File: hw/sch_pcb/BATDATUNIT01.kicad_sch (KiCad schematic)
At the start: 45 parts, among them J1 USBC_USB4105-GF-A, J2 46436-9327, U1 FT260Q-T, U2 USBLC6-2SC6, U3 TCA4307, U4 SHT35-DIS, U5 PCA9541ABS/01

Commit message: WIP, schematic improvements, bigger page, reststructualized
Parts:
- added BZ1: LET9032ES-03L, MLAB_BUZZER:MagneticBuzzer_LET9032ES-03L-2.7-16-R, symbol Device:Buzzer
- added C26, C27, C36, C44, C5, C6, C60, C7: 100n, Capacitor_SMD:C_0805_2012Metric, symbol Device:C_Small
- added C30, C33: 15p, Capacitor_SMD:C_0805_2012Metric, symbol Device:C_Small
- added C40: 10u, Capacitor_SMD:C_0805_2012Metric, symbol Device:C_Small
- added C43: 4u7, Capacitor_SMD:C_0805_2012Metric, symbol Device:C_Small
- added C47: 1u, Capacitor_SMD:C_0805_2012Metric, symbol Device:C_Small
- added D16 (x3): ORANGE, Mlab_D:SMD_LED_RIGHT_KINGBRIGHT_1605, symbol Device:LED_Small
- added IC1: MAX14502AETL+, Mlab_IO:QFN40P500X500X80-41N, symbol MLAB_IO:MAX14502AETL+
- added J22: HEADER_2x03, Mlab_Pin_Headers:SMD_2x03, symbol MLAB_HEADER:HEADER_2x03
- added J9: SD_Card-FPS009-4200-0, Mlab_CON:FPS009-4200-0, symbol MLAB_CONNECTORS:SD_Card-FPS009-4200-0
- added JP2: Jumper_3_Bridged12, Jumper:SolderJumper-3_P1.3mm_Bridged2Bar12_RoundedPad1.0x1.5mm, symbol Jumper:SolderJumper_3_Bridged12
- added Q1, Q2, Q3, Q4: BC817-25, Package_TO_SOT_SMD:SOT-23-3, symbol Device:Q_NPN_BEC
- added R1: 6.19k, Resistor_SMD:R_0805_2012Metric, symbol Device:R_Small
- added R16, R17, R28, R29, R55, R56: 1k, Resistor_SMD:R_0805_2012Metric, symbol Device:R_Small
- added R17 (x6): 100R, Resistor_SMD:R_0805_2012Metric, symbol SPACEDOS02A_PCB01A-rescue:R-device-DATALOGGER01A-rescue-CCP2019V01A-rescue-SPAC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
- added R23 (x2), R58, R59, R60: 10k, Resistor_SMD:R_0805_2012Metric, symbol Device:R_Small
- added R54 (x3): 270R, Resistor_SMD:R_0805_2012Metric, symbol Device:R_Small
- added SW3: SKRTLAE010, Mlab_SW:SKRT, symbol MLAB_SW:SW_Push_shield
- added SW3, SW4: KMT031, Mlab_SW:KMT031 NGJ LHS C&K, symbol Switch:SW_Push
- added U10: ATMEGA1284P-AU, Package_QFP:TQFP-44_10x10mm_P0.8mm, symbol SPACEDOS01A_PCB01A-rescue:ATMEGA1284P-AU-atmel-DATALOGGER01A-rescue-CCP2019V01A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
- added U11: PCF85263A, Package_SO:TSSOP-10_3x3mm_P0.5mm, symbol MLAB_IO:PCF85263A
- added U12: TMUX1574DYYR, Mlab_IO:SOT-23-16 THIN, symbol MLAB_IO:TMUX1574DYYR
- added U6: AT24CS64-SSHM, Package_SO:SOIC-8_3.9x4.9mm_P1.27mm, symbol Memory_EEPROM:AT24CS64-SSHM
- added Y1: 8 MHz, Crystal:Crystal_SMD_3225-4Pin_3.2x2.5mm, symbol Device:Crystal_GND24_Small
- added Y2: ABS07-120-32.768KHZ-T, Mlab_XTAL:ABS07, symbol SPACEDOS01A_PCB01A-rescue:Crystal-device-DATALOGGER01A-rescue-CCP2019V01A-rescue
- R20, R21: symbol SPACEDOS01A_PCB01A-rescue:R-device-DATALOGGER01A-rescue-CCP2019V01A-rescue -> Device:R_Small
- renumbered C3 to C4, J2 to J4, R1 to R13, R10 to R14, R2 to R15, R11 to R18, R5 to R26, R16 to R27, R6 to R31, R7 to R32, TP2 to TP1, U3 to U10, U1 to U3, U5 to U4, U4 to U6
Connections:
- net +3.3V: now also BZ1.1 (-), C26.1, C27.1, C36.1, C47.1, C6.1, D16.2 (A), D16.2 (A), D16.2 (A), IC1.39 (VCC), IC1.5 (VIO), IC1.9 (~{RST}), J22.2, JP2.1 (A), R23.2, R58.1, R59.1, U10.17 (VCC), U10.27 (AVCC), U10.38 (VCC), U10.5 (VCC), U11.10 (VDD), U12.16 (VDD), U6.8 (VCC)
- net DET_I2C_EN: now also U10.42 ((PCINT10/AIN0/INT2)PB2)
- net EXT_A0: now also U10.37 ((PCINT0/ADC0)PA0)
- net EXT_A1: now also U10.36 ((PCINT1/ADC1)PA1)
- net EXT_B0: now also U10.40 ((PCINT8/T0/XCK)PB0)
- net EXT_B1: now also U10.41 ((PCINT9/CLKO/T1)PB1)
- net EXT_C0: now also U10.25 ((PCINT22/TOSC1)PC6)
- net EXT_C1: now also U10.26 ((PCINT23/TOSC2)PC7)
- net EXT_MISO: now also U12.6 (S2B)
- net EXT_MOSI: now also U12.3 (S1B)
- net EXT_RX: now also U10.11 ((PCINT26/RXD1/INT0)PD2)
- net EXT_SCLK: now also U12.10 (S3B)
- net EXT_TX: now also U10.12 ((PCINT27/TXD1/INT1)PD3)
- net GND: now also C26.2, C27.2, C30.2, C33.2, C36.2, C40.2, C44.2, C47.2, C5.2, C6.2, C60.2, C7.2, IC1.18 (GND_1), IC1.24 (GND_2), IC1.26 (GND_3), IC1.33 (CCRD_PRST), IC1.35 (N.C._1), IC1.36 (N.C._2), IC1.37 (GND_4), IC1.4 (ADD), IC1.41 (GND_5), J22.6, J9.12 (SHELL1), J9.3 (VSS), J9.6 (VSS), JP2.3 (B), Q1.2 (E), Q2.2 (E), Q3.2 (E), Q4.2 (E), R1.2, R23.1, R56.2, R60.1, SW3.2, SW3.2, SW3.GND (SHIELD), SW4.1, U10.18 (GND), U10.28 (GND), U10.39 (GND), U10.6 (GND), U11.5 (GND), U12.15 (~{EN}), U12.8 (GND), U6.1 (A0), U6.2 (A1), U6.3 (A2), U6.4 (GND), U6.7 (WP), Y1.2, Y1.4
- net MCU_RXD: now also U10.9 ((PCINT24/RXD0)PD0)
- net MCU_TXD: now also U10.10 ((PCINT25/TXD0)PD1)
- net RST#: now also C43.2
- net SCL_I2C: now also IC1.2 (SCL), U11.7 (SCL), U6.6 (SCL)
- net SCL_MCU: now also U10.19 ((PCINT16/SCL)PC0)
- net SDA_I2C: now also IC1.3 (SDA), U11.6 (SDA), U6.5 (SDA)
- net SDA_MCU: now also U10.20 ((PCINT17/SDA)PC1)
- net USB_D+: now also IC1.22 (CD+)
- net USB_D-: now also IC1.21 (CD-)
- net USB_FTDI_D+: now also IC1.20 (HD+)
- net USB_FTDI_D-: now also IC1.19 (HD-)
- net VBUS: now also R55.1
- new net: IC1.28 (KVBUS), R55.2, R56.1
- new net: D16.1 (K), R54.1 (x3)
- new net: Q2.3 (C), R54.2
- new net: J9.1 (CD/DAT3), R17.2
- new net: C40.1, C44.1, U10.29 (AREF)
- new net: C30.1, U10.7 (XTAL2), Y1.1
- new net: C33.1, U10.8 (XTAL1), Y1.3
- new net: C60.1, U11.3 (VBAT)
- new net: Q3.1 (B), R28.2
- new net: IC1.1 (I2C_SEL), JP2.2 (C)
- new net: J9.7 (DAT0), R17.1
- new net: J9.9 (DAT2), R17.2
- new net: Q3.3 (C), R54.2
- new net: J9.2 (CMD), R17.2
- new net: BZ1.2 (+), Q4.3 (C)
- new net: J9.5 (CLK), R17.2
- new net: J9.8 (DAT1), R17.1
- new net: Q1.1 (B), R16.2
- new net: Q1.3 (C), R54.2
- new net: Q4.1 (B), R29.2
- new net: U11.1 (OSCI), Y2.2
- new net: U11.2 (OSCO), Y2.1
- new net: Q2.1 (B), R17.2
- new net 3v3_SD: IC1.40 (VSD), J9.4 (VDD)
- new net 3v3_SD_CTRL: U10.22 ((PCINT19/TMS)PC3)
- new net BTN_USER_A: R58.2, SW3.1, U10.31 ((PCINT6/ADC6)PA6)
- new net BTN_USER_B: R59.2, SW3.1, U10.30 ((PCINT7/ADC7)PA7)
- new net CCLK: IC1.32 (CCLK1), R17.1
- new net CCMD: IC1.34 (CCMD1), R17.1
- new net CDAT0: IC1.13 (CDAT1_0), R17.2
- new net CDAT1: IC1.12 (CDAT1_1), R17.2
- new net CDAT2: IC1.11 (CDAT1_2), R17.1
- new net CDAT3: IC1.10 (CDAT1_3), R17.1
- new net CLDO: C5.1, IC1.38 (CLDO)
- new net CS_SD: IC1.14 (HDAT1_3), U10.44 ((PCINT12/OC0B/~{SS})PB4)
- new net LED_U1: R16.1, U10.13 ((PCINT28/XCK1/OC1B)PD4)
- new net LED_U2: R28.1, U10.14 ((PCINT294/OC1A)PD5)
- new net LED_U3: R17.1, U10.15 ((PCINT30/OC2B/ICP)PD6)
- new net MISO_MCU: J22.1, U10.2 ((PCINT14/MISO)PB6), U12.7 (D2)
- new net MISO_SD: IC1.17 (HDAT1_0), U12.5 (S2A)
- new net MOSI_MCU: J22.4, U10.1 ((PCINT13/MOSI)PB5), U12.4 (D1)
- new net MOSI_SD: IC1.31 (HCMD1), U12.2 (S1A)
- new net RREF: IC1.27 (RREF), R1.1
- new net RST#_P: C43.1, J22.5, R23.1, SW4.2, U10.4 (~{RESET})
- new net SCLK_MCU: J22.3, U10.3 ((PCINT15/SCK)PB7), U12.9 (D3)
- new net SCLK_SD: IC1.29 (HCLK1), U12.11 (S3A)
- new net SPI_MUX_SEL: R60.2, U10.21 ((PCINT18/TCK)PC2), U12.1 (SEL)
- new net VTM: C7.1, IC1.23 (VTM)
- new net buzzer: R29.1, U10.16 ((PCINT31/OC2A)PD7)
- new net mode: IC1.8 (MODE), R23.2, U10.43 ((PCINT11/AIN1/OC0)PB3)
- no-connect marks 26 -> 43
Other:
- removed sheet mcu
- note added: "ATmega 1284p microcontroller"
- note added: "Connector for detector board"
- note added: "FTDI (USB to UART and I2C)"
- note added: "I2C master selector (from FTDI or ATmega)"
- note added: "I2C sensors and accessories (hygrometer, altimeter, eeprom, RTC)"
- note added: "Mechanical"
- note added: "SD card interface (USB to SDcard reader and USB-bridge to FTDI)"
- note added: "SPI-MUX (switching SPI from MCU to SDcard or to detector ext. connector)"
- note added: "USB-C connector and ESD protection"
- note added: "User interface (LED indicators, Buttons)"
- note removed: "USB-C connector"
- moved on the sheet: C4, C?, D1, D2, FID1, FID2, FID3, FID4, H1, H2, H3, H4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

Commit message: Updates in schematics, improved readability
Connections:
- net EXT_I2C_EN: now reaches U10.23 ((PCINT20/TDO)PC4)
- net EXT_I2C_EN: now also R21.1, U10.1 (EN)
- net EXT_PWR_5v_EN: now reaches U10.35 ((PCINT2/ADC2)PA2)
- removed net DET_I2C_EN: R21.1, U10.1 (EN), U10.42 ((PCINT10/AIN0/INT2)PB2)
- net EXT_I2C_SCL renamed SCL_OUT
- net EXT_I2C_SDA renamed SDA_OUT
- net EXT_MISO renamed MISO_OUT
- net EXT_MOSI renamed MOSI_OUT
- net EXT_SCLK renamed SCLK_OUT
- net MCU_RXD renamed USB_TXD
- net MCU_TXD renamed USB_RXD
- new net EXT_PWR_3v3_EN: U10.42 ((PCINT10/AIN0/INT2)PB2)
- no-connect marks 43 -> 42
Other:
- company: MLAB.cz -> MLAB.cz, roman-dvorak
- moved on the sheet: C?, D1, D2, IC1, JP1, JP2, R13, R14, R15, R18, R23, R26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

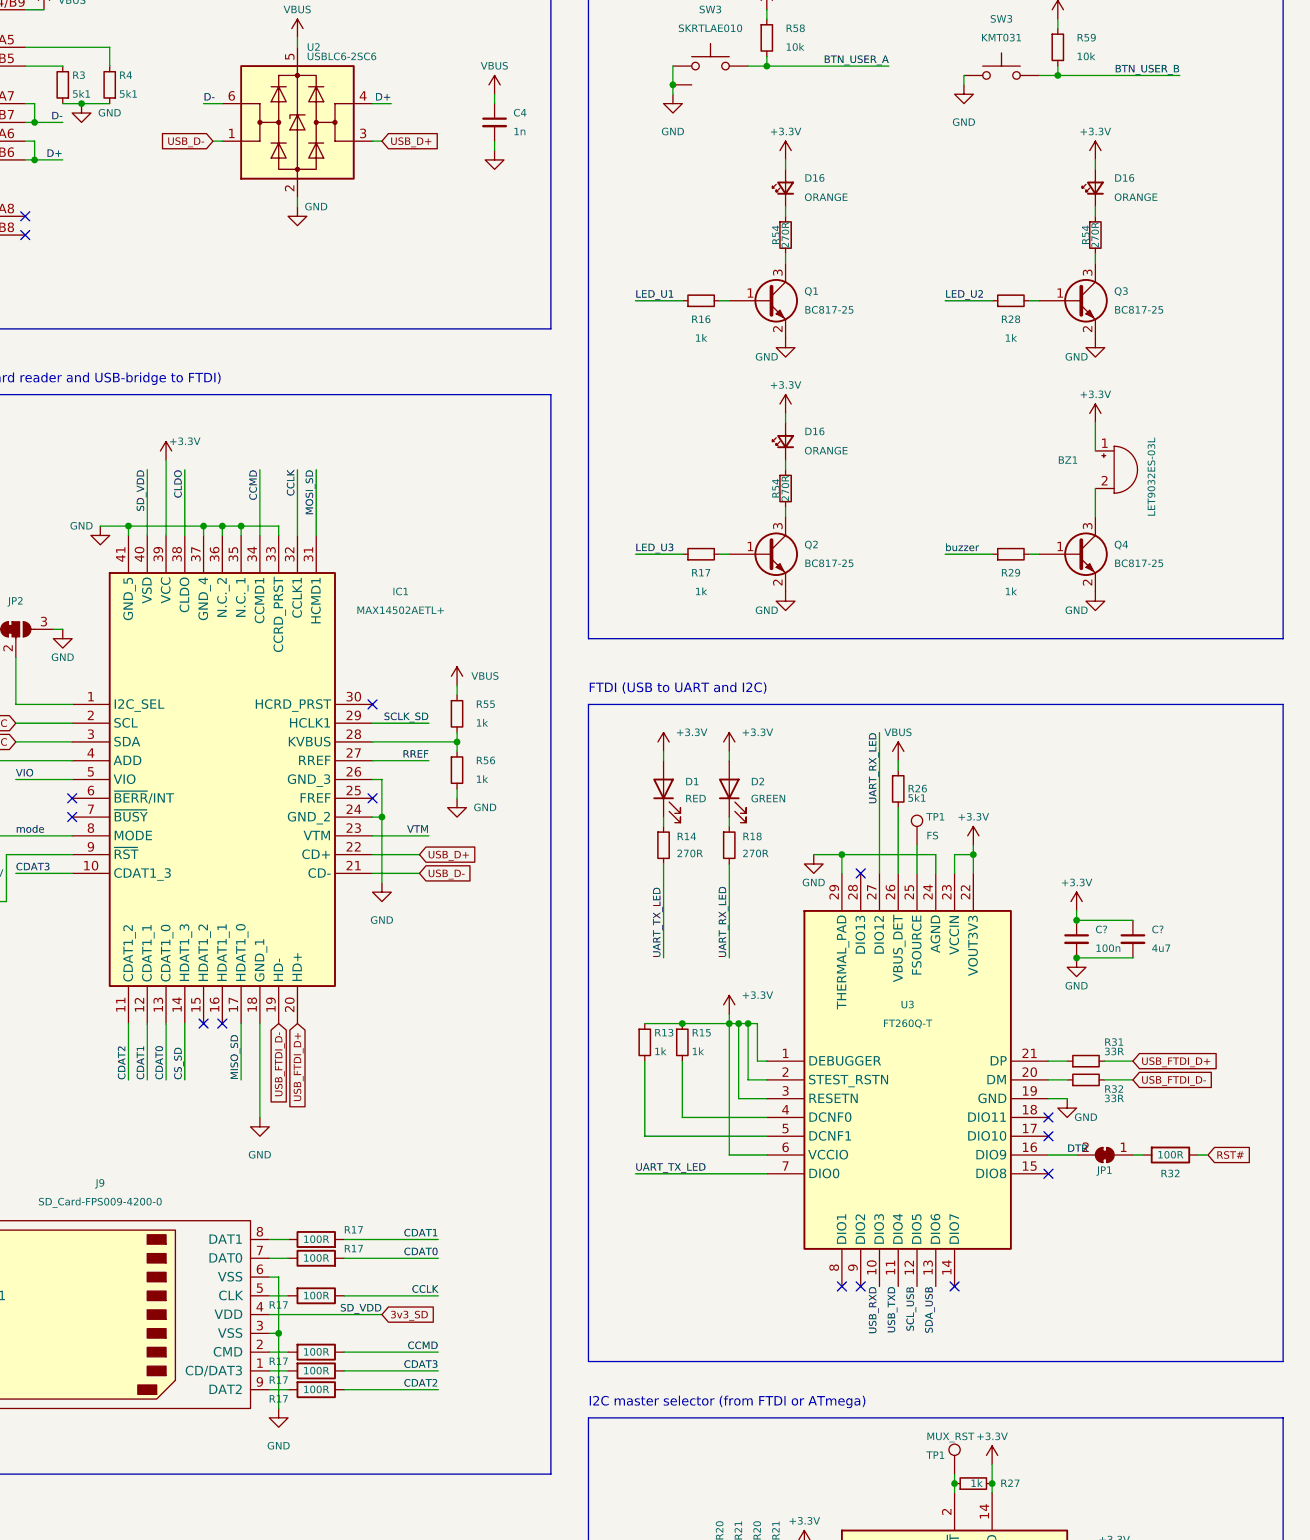
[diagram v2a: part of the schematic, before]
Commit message: minor updates, update kibot
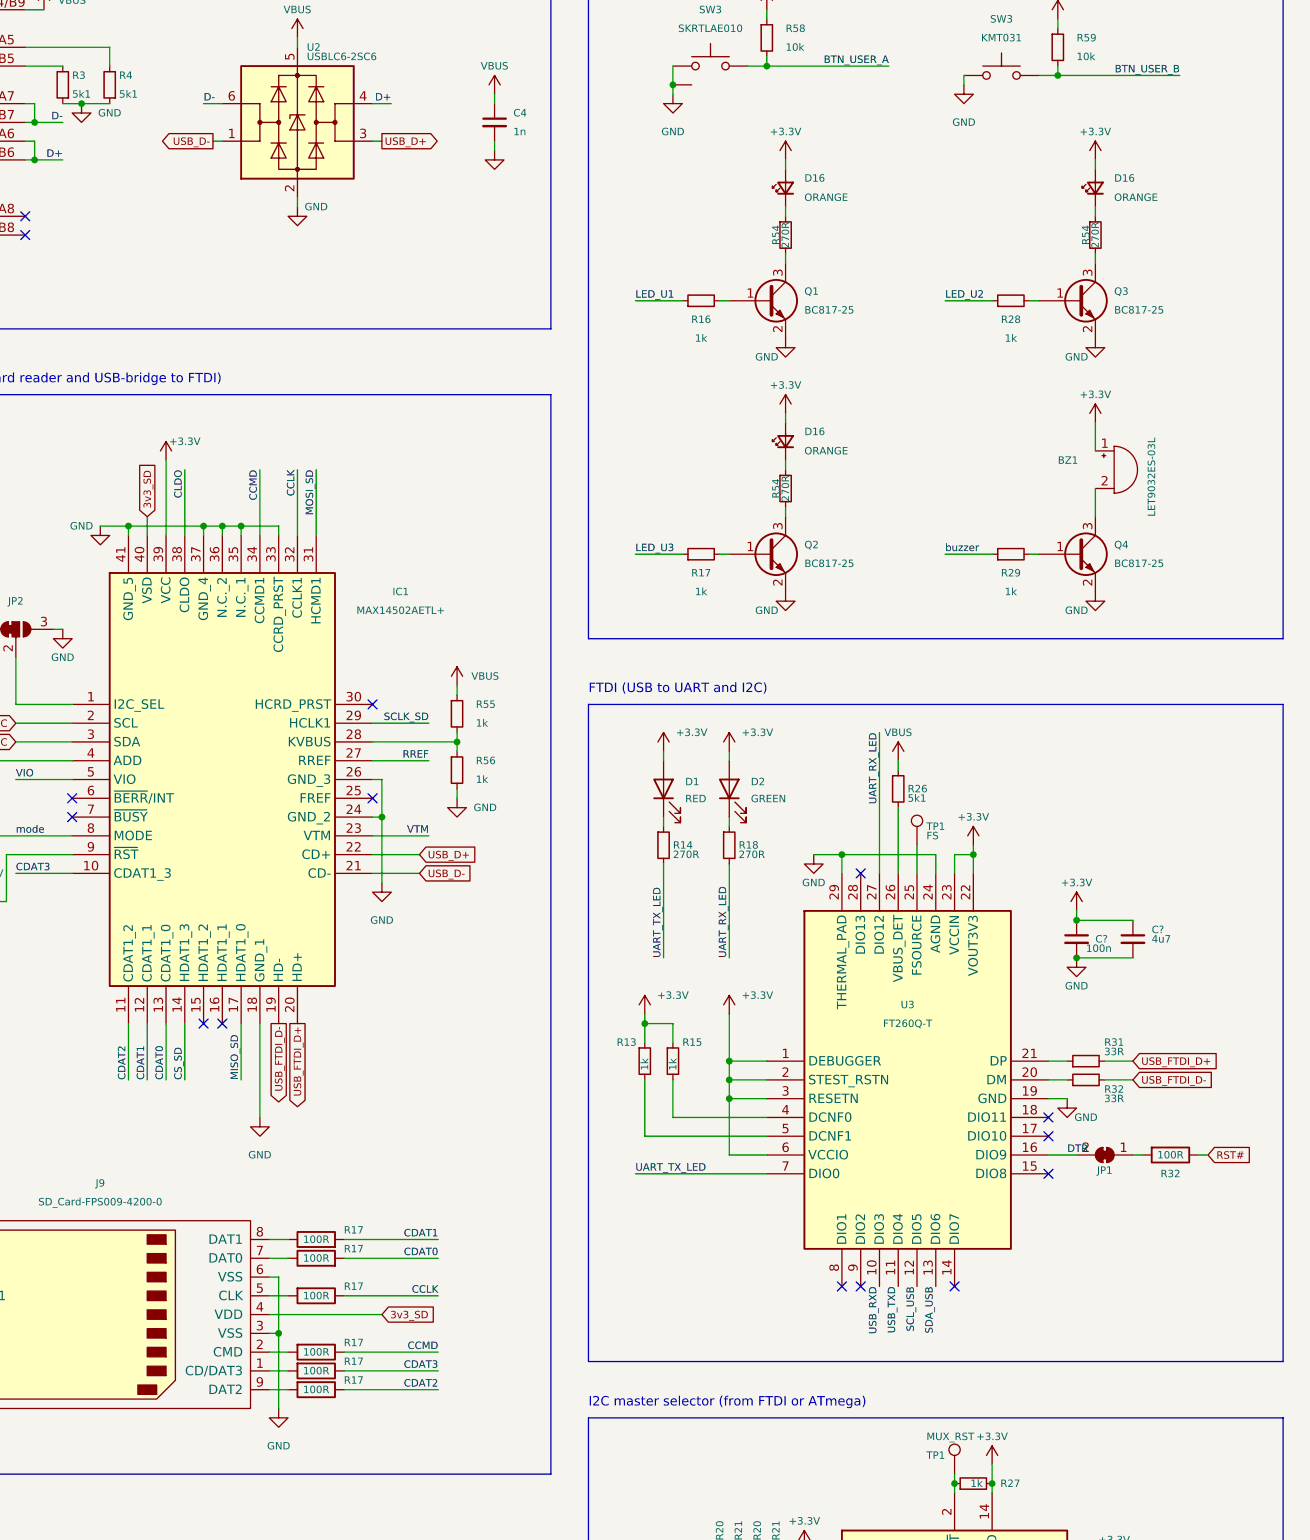
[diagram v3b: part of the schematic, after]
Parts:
- D1: UST_ID (none) -> 65481f96462c6d9e72056b54
- D16: UST_ID (none) -> 65481fdd462c6d9e72056b6a
- D2: UST_ID (none) -> 65481f0c462c6d9e72056b3d
- IC1: UST_ID (none) -> 6548165f462c6d9e720569f7
- J4: UST_ID (none) -> 65481d4a462c6d9e72056b06
- R1: UST_ID (none) -> 6548142e462c6d9e72056976
- R14, R18, R54: UST_ID (none) -> 5c70984512875079b91f8983
- SW3: UST_ID (none) -> 65481517462c6d9e720569b4
- U10: UST_ID (none) -> 6087a3f3128750769ee58f03
- U12: UST_ID (none) -> 65481983462c6d9e72056a6d
- U3: UST_ID (none) -> 65481702462c6d9e72056a21
- U4: UST_ID (none) -> 65481909462c6d9e72056a4a
- Y1: UST_ID (none) -> 65481c4c462c6d9e72056ac8
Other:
- moved on the sheet: R13, R15

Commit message: updated power button connection
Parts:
- added C47: 10u, symbol Device:C_Small
- added D16: BAS70-04, Package_TO_SOT_SMD:SOT-23, symbol Device:D_Schottky_Dual_Series_AKC
- added JP8: SolderJumper_2_Open, Jumper:SolderJumper-2_P1.3mm_Open_RoundedPad1.0x1.5mm, symbol Jumper:SolderJumper_2_Open
- added R17: 100R, Resistor_SMD:R_0805_2012Metric, symbol SPACEDOS02A_PCB01A-rescue:R-device-DATALOGGER01A-rescue-CCP2019V01A-rescue-SPAC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
- added R20, R21: 1k, Resistor_SMD:R_0805_2012Metric, symbol Device:R_Small
- added R59: 10k, Resistor_SMD:R_0805_2012Metric, symbol Device:R_Small
- added R74: 10M, symbol Device:R_Small
- added SW4: SKRTLAE010, Mlab_SW:SKRT, symbol MLAB_SW:SW_Push_shield
- R23: now fitted
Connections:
- net +3.3V: now also R20.2, R21.2, R59.1
- net +BATT: now also R17.2
- net GND: now also SW4.2, SW4.GND (SHIELD)
- net SCL_OUT: now also R20.1
- net SDA_OUT: now also R21.1
- net EXT_DETECTION_MCU: now reaches U10.34 ((PCINT3/ADC3)PA3)
- net EXT_DETECTION_MCU: now also D16.1 (A), R59.2
- net at C60.1, U11.3 (VBAT): now also JP8.2 (B)
- net EXT_DETECTION: now reaches J4.D6
- net EXT_DETECTION: now also C47.1, D16.3 (common), R74.1
- new net: JP8.1 (A), R17.1
- new net EXT_DETECTION_CHARGER: C47.2, R74.2, SW4.1
- no-connect marks 42 -> 41
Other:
- note added: "Auto-power up wiring"
- note added: "Enabled by default (EN - high)"
- note added: "I2C buffer, allows to unconnect external I2C"
- moved on the sheet: C60, J4, R13, R15, R21, R58, R59, SW3, U10
